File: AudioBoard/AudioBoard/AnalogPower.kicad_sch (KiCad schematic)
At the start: 0 parts

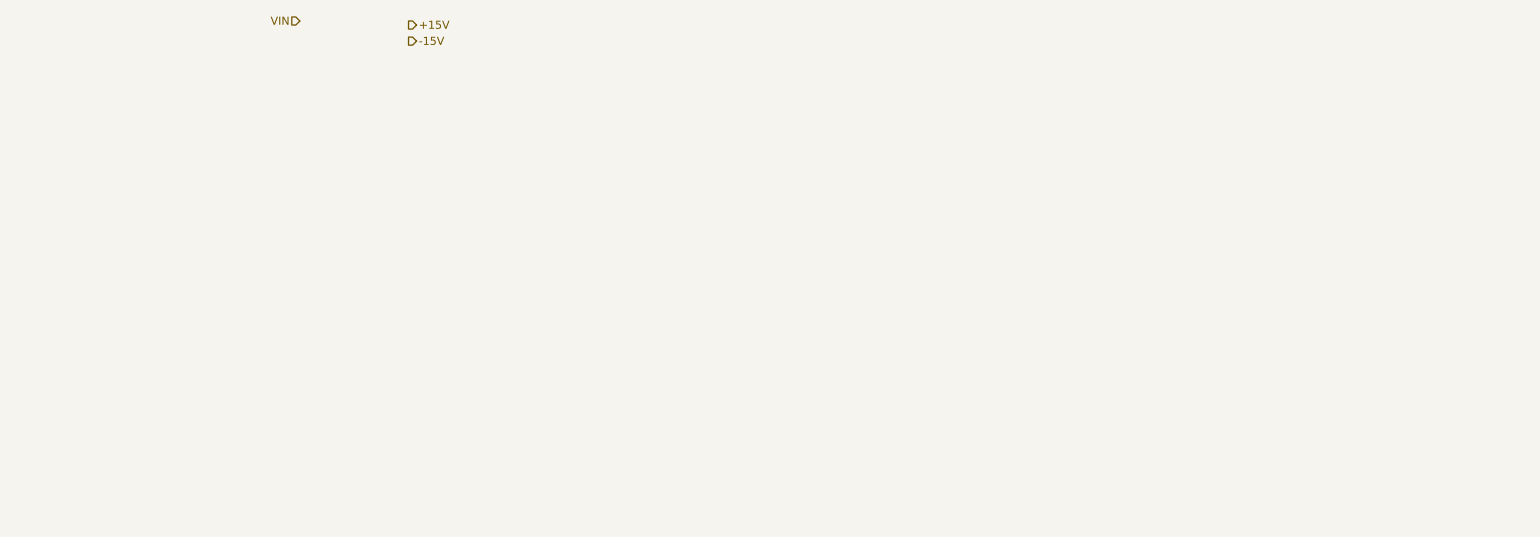
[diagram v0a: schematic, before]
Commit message: added power protection, dcdc modules
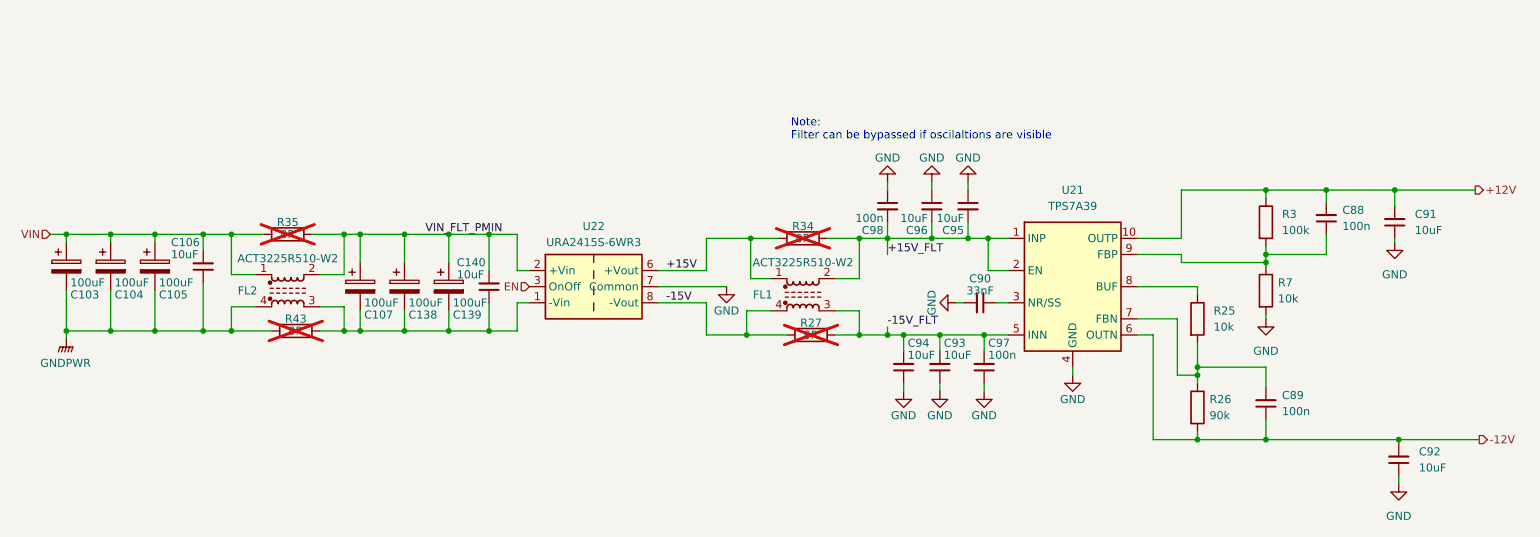
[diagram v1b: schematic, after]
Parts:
- added C103, C104, C105, C107, C138, C139: 100uF, symbol Device:C_Polarized
- added C106, C140, C91, C92, C93, C94, C95, C96: 10uF, Capacitor_SMD:C_0402_1005Metric, symbol Device:C_Small
- added C88, C89, C97, C98: 100n, Capacitor_SMD:C_0402_1005Metric, symbol Device:C_Small
- added C90: 33nF, Capacitor_SMD:C_0805_2012Metric_Pad1.18x1.45mm_HandSolder, symbol Device:C_Small
- added FL1, FL2: ACT3225R510-W2, Inductor_SMD:L_CommonModeChoke_Coilank_ACM3225, symbol Filter:Choke_CommonMode_FerriteCore_1243
- added R25, R7: 10k, symbol Device:R
- added R26: 90k, symbol Device:R
- added R27, R34, R35, R43: 0R, Resistor_SMD:R_0402_1005Metric, symbol Device:R
- added R3: 100k, symbol Device:R
- added U21: TPS7A39, Package_SON:Texas_S-PVSON-N10_ThermalVias, symbol Regulator_Linear:TPS7A39
- added U22: URA2415S-6WR3, Converter_DCDC:Converter_DCDC_TRACO_TEC2-12xxWI_24xxWI_48xxWI_THT, symbol Converter_DCDC:ITQ2415S
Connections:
- net +15V: now also FL1.1, R34.1, U22.6 (+Vout)
- net -15V: now also FL1.4, R27.1, U22.8 (-Vout)
- net VIN: now also C103.1, C104.1, C105.1, C106.2, FL2.1, R35.1
- new net: C107.2, C138.2, C139.2, C140.1, FL2.3, R43.2, U22.1 (-Vin)
- new net: C90.1, U21.3 (NR/SS)
- new net: C89.2, R25.2, R26.1, U21.7 (FBN)
- new net: R25.1, U21.8 (BUF)
- new net: C88.1, R3.2, R7.1, U21.9 (FBP)
- new net +12V: C88.2, C91.2, R3.1, U21.10 (OUTP)
- new net +15V_FLT: C95.2, C96.2, C98.2, FL1.2, R34.2, U21.1 (INP), U21.2 (EN)
- new net -12V: C89.1, C92.2, R26.2, U21.6 (OUTN)
- new net -15V_FLT: C93.2, C94.2, C97.2, FL1.3, R27.2, U21.5 (INN)
- new net EN: U22.3 (OnOff)
- new net GND: C90.2, C91.1, C92.1, C93.1, C94.1, C95.1, C96.1, C97.1, C98.1, R7.2, U21.11 (GND), U21.4 (GND), U22.7 (Common)
- new net GNDPWR: C103.2, C104.2, C105.2, C106.1, FL2.4, R43.1
- new net VIN_FLT_PMIN: C107.1, C138.1, C139.1, C140.2, FL2.2, R35.2, U22.2 (+Vin)
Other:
- note added: "Note: Filter can be bypassed if oscilaltions are visible"

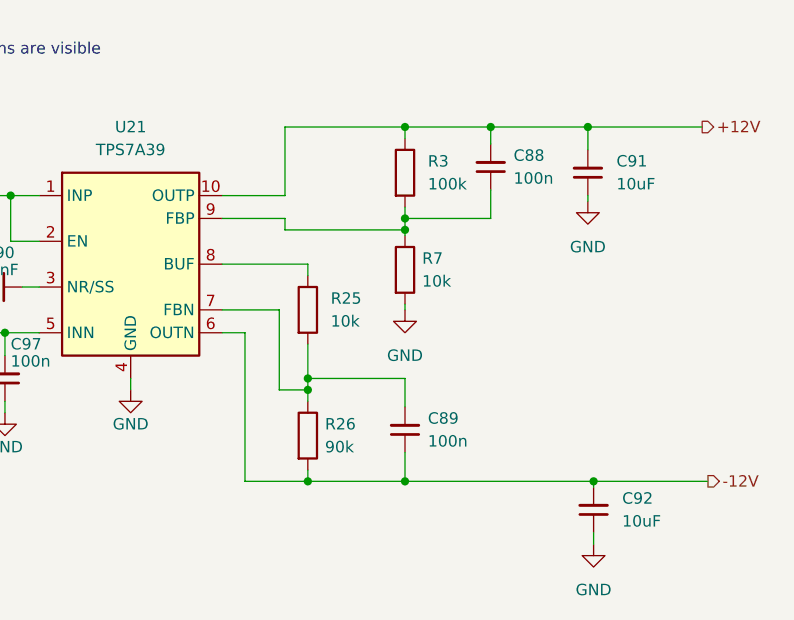
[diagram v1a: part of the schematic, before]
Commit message: assigned footprint to elements lcsc parts
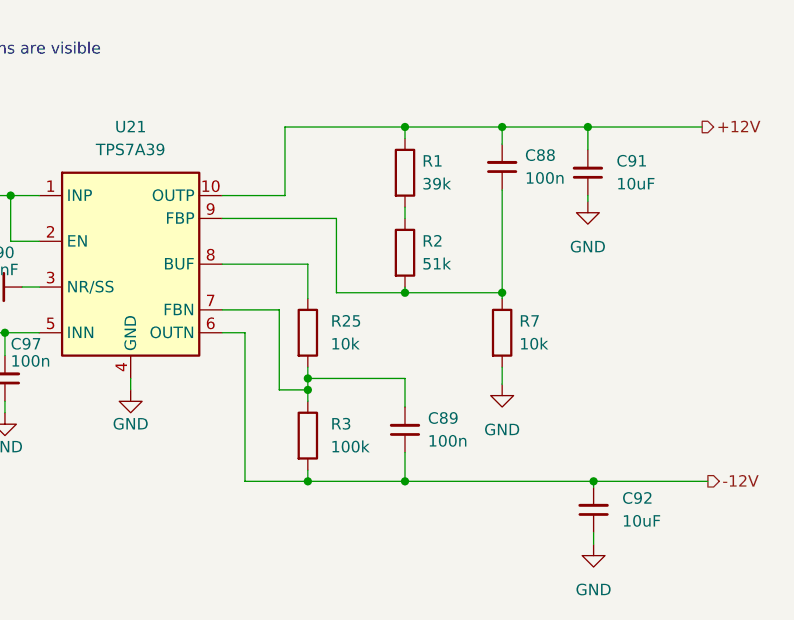
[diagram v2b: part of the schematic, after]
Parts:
- removed R26: 90k, symbol Device:R
- added R1: 39k, Resistor_SMD:R_0603_1608Metric, symbol Device:R
- added R2: 51k, Resistor_SMD:R_0603_1608Metric, symbol Device:R
- C103, C104, C105, C107, C138, C139: footprint (none) -> Capacitor_SMD:CP_Elec_5x5.4; JLCPCB (none) -> C48970701; LCSC Part (none) -> C48970701
- FL1, FL2: JLCPCB (none) -> C49420293; LCSC Part (none) -> C49420293
- R25, R7: footprint (none) -> Resistor_SMD:R_0603_1608Metric; JLCPCB (none) -> C4184; LCSC Part (none) -> C4184
- R27, R34, R35, R43: footprint Resistor_SMD:R_0402_1005Metric -> Resistor_SMD:R_0603_1608Metric_Pad0.98x0.95mm_HandSolder; JLCPCB (none) -> C21189; LCSC Part (none) -> C21189
- R3: footprint (none) -> Resistor_SMD:R_0402_1005Metric; JLCPCB (none) -> C25741; LCSC Part (none) -> C25741
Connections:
- net +12V: now also R1.1; no longer R3.1
- net -12V: now also R3.2
- net at C89.2, R25.2, U21.7 (FBN): now also R3.1
- net at C88.1, R7.1, U21.9 (FBP): now also R2.2; no longer R3.2
- new net: R1.2, R2.1
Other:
- moved on the sheet: C88, R25, R7

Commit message: added bias voltage buffer, fixed fsw shift reg input filter
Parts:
- R27, R34, R35, R43: now left out of the parts list
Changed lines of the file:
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@@
 		(body_style 1)
 		(exclude_from_sim no)
-		(in_bom yes)
+		(in_bom no)
 		(on_board yes)
 		(in_pos_files yes)
@@
 		(body_style 1)
 		(exclude_from_sim no)
-		(in_bom yes)
+		(in_bom no)
 		(on_board yes)
 		(in_pos_files yes)
@@
 		(body_style 1)
 		(exclude_from_sim no)
-		(in_bom yes)
+		(in_bom no)
 		(on_board yes)
 		(in_pos_files yes)
@@
 		(body_style 1)
 		(exclude_from_sim no)
-		(in_bom yes)
+		(in_bom no)
 		(on_board yes)
 		(in_pos_files yes)

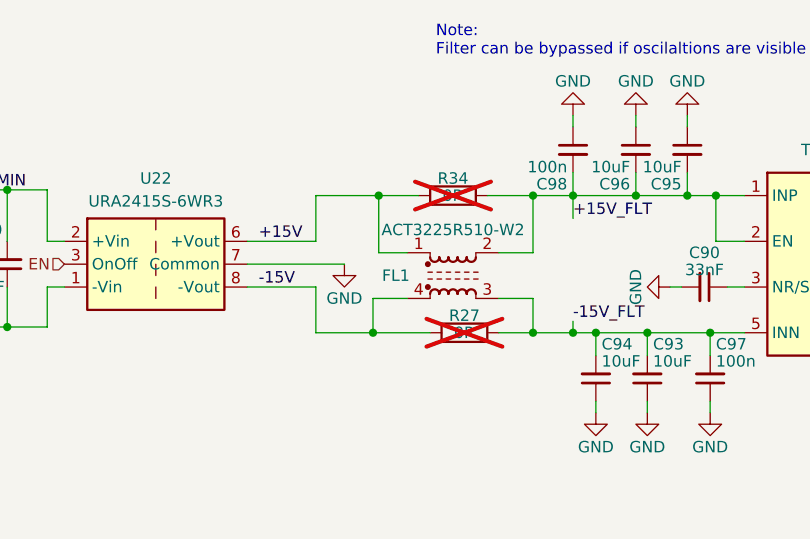
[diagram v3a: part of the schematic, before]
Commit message: modified clamping diodes on inputs, added exp pedal input filter, added ideas to instrument input filter redesign
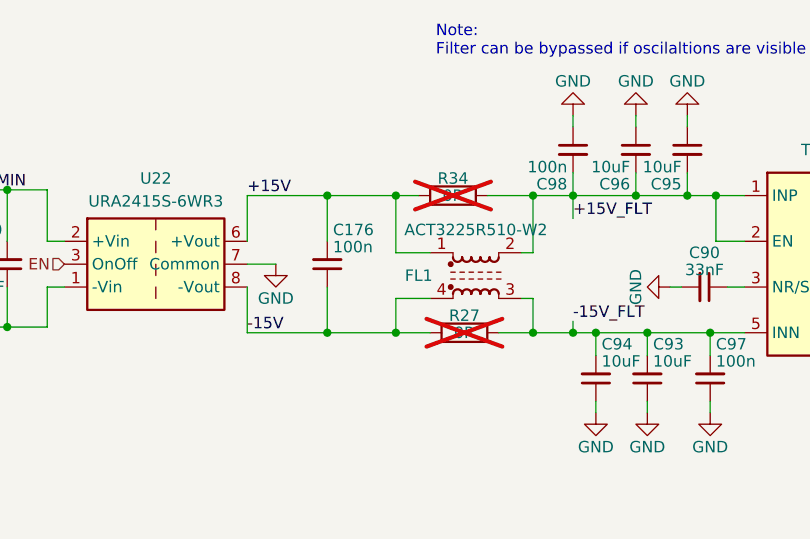
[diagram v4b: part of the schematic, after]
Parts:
- added C176: 100n, Capacitor_SMD:C_0402_1005Metric, symbol Device:C_Small
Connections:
- net +15V: now also C176.2
- net -15V: now also C176.1
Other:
- moved on the sheet: FL1
